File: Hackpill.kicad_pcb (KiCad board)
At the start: 2 copper layers, 63.2 x 30.5 mm, 34 parts, among them J1 Conn_01x04, J2 USB_C_Receptacle_USB2.0_16P, J3 Conn_01x22, J4 Conn_01x22, SW1 SW_Push, U1 STM32F042C6Tx, U2 AMS1117-3.3, U3 USBLC6-2SC6

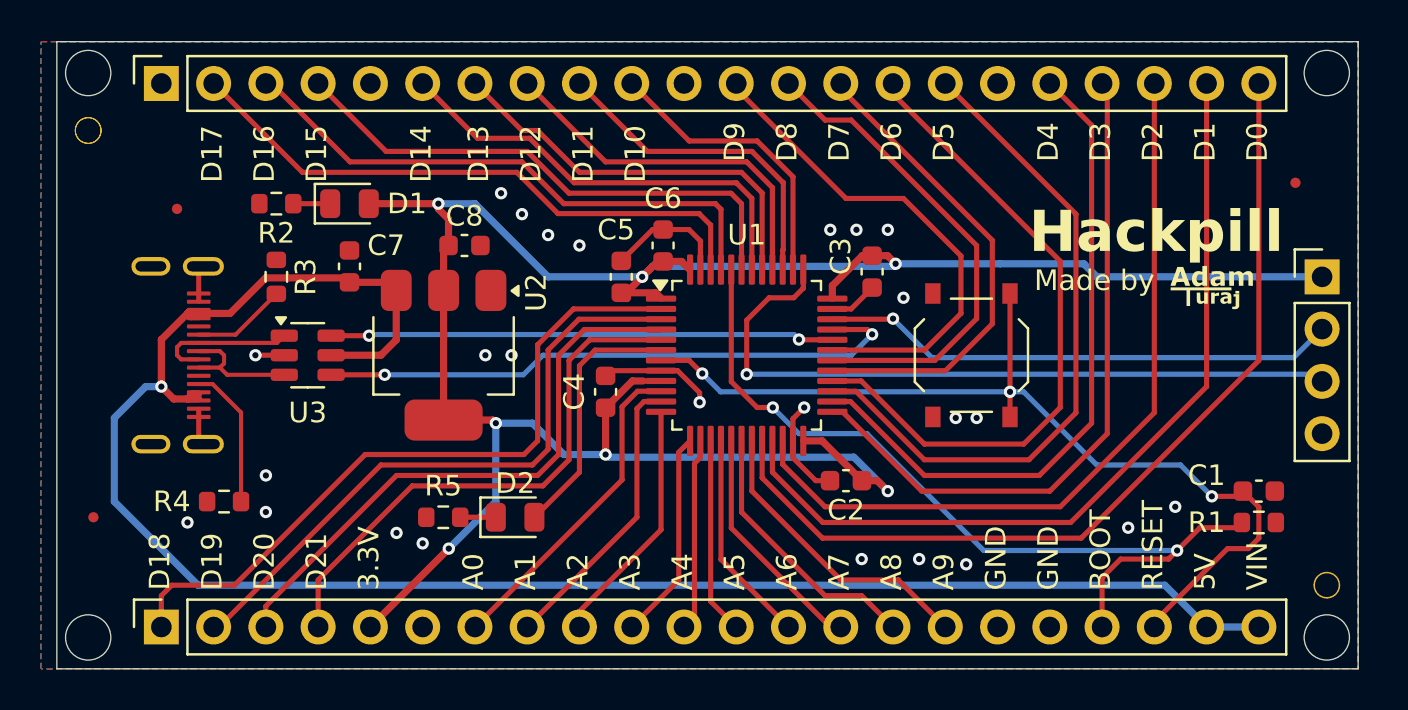
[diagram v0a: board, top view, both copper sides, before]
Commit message: Add diode to USB, rename files, add prod files
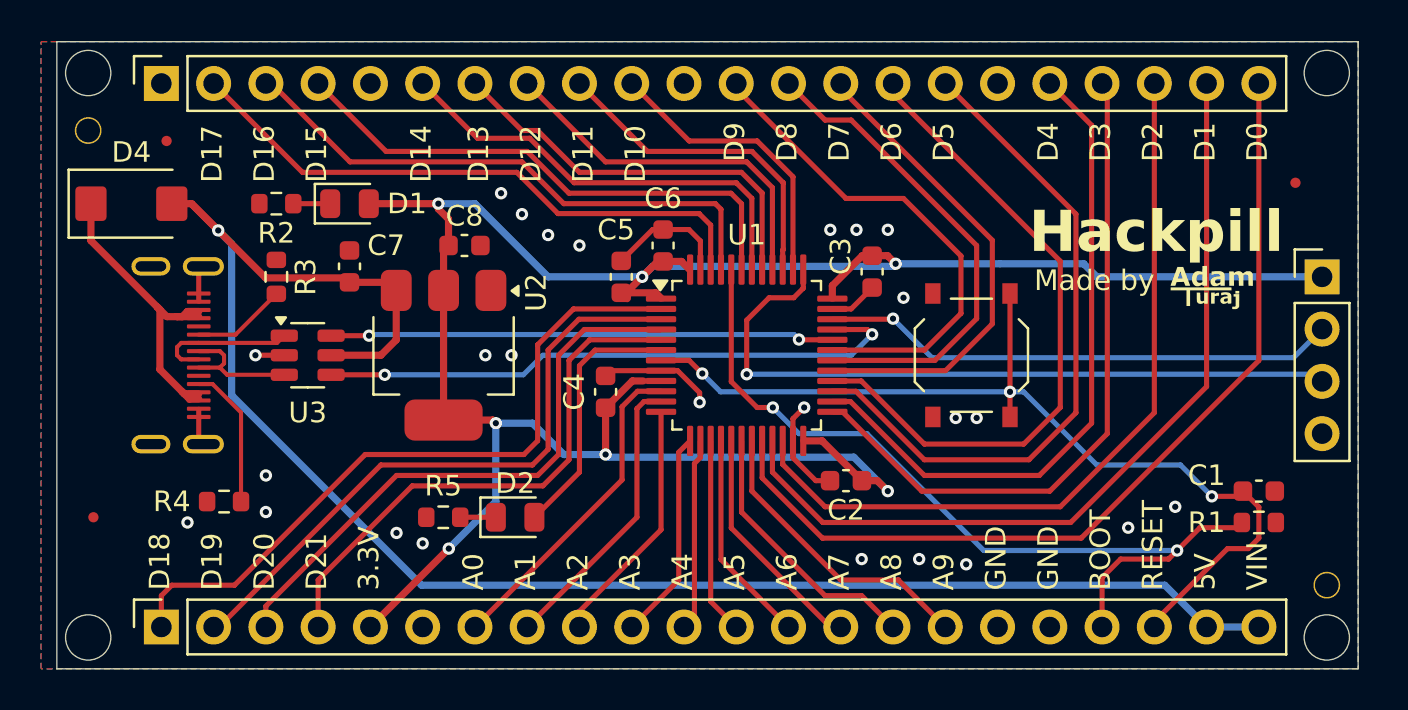
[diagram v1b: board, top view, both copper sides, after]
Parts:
- removed ?: , 
- added D4: SS14, Diode_SMD:D_SMA, F.Cu at (129.1, 93.0)
- moved REF** 3.34 mm to (130.8, 89.9)
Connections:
- J2 pad A4: +5V -> Net-(D4-A)
- J2 pad A9: +5V -> Net-(D4-A)
- J2 pad B4: +5V -> Net-(D4-A)
- J2 pad B9: +5V -> Net-(D4-A)
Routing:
- net Net-(D4-A): track 0.00 -> 16.1 mm
- net +5V: track 90.3 -> 83.4 mm

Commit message: Change clearence, update footprint, add README, add schematic, remove config file
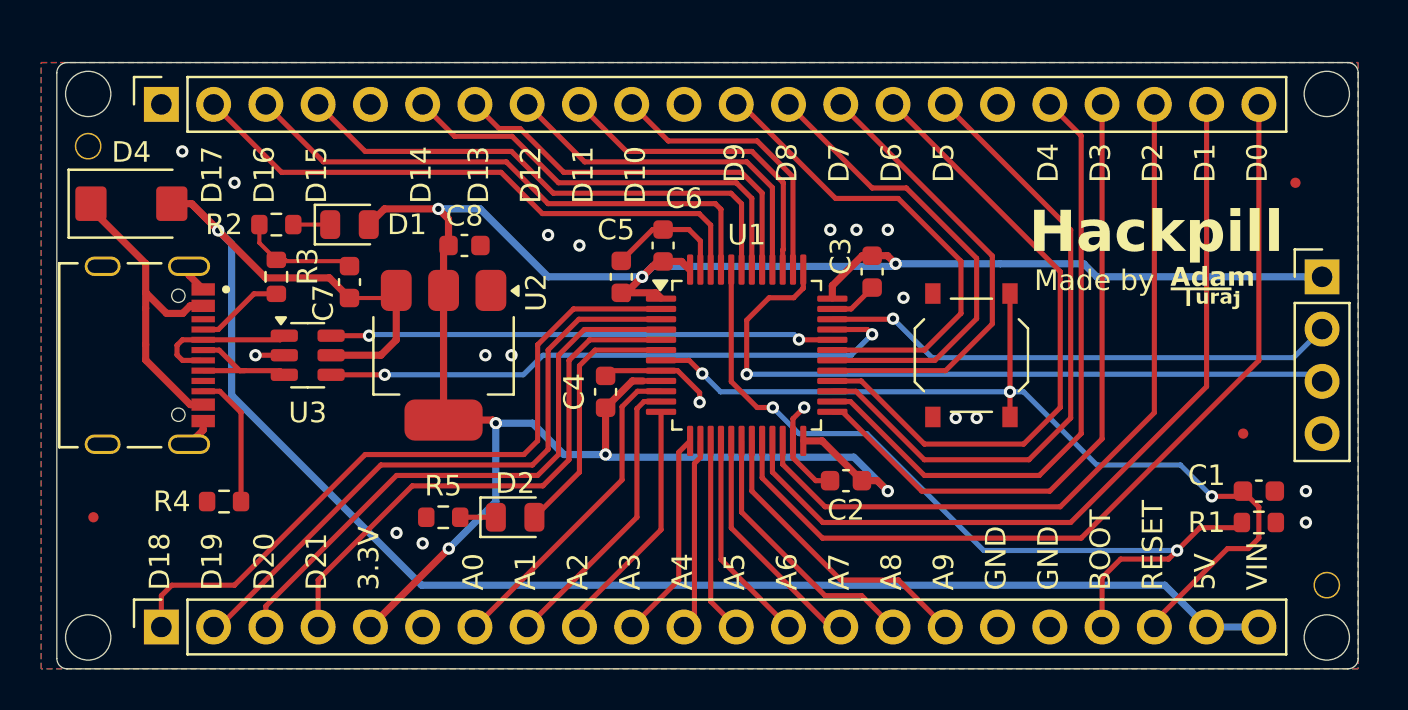
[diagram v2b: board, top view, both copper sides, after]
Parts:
- J2: footprint Connector_USB:USB_C_Receptacle_Hanbo_16P_TopMnt_Horizontal -> Connector_USB:USB_C_Receptacle_Shouhan_16P_TopMnt_Horizontal
- moved REF** 54.2 mm to (183.1, 104.1)
- moved J2 1.27 mm to (128.8, 100.3)
- moved D1 1.02 mm to (139.7, 94.0)
- moved J4 1.02 mm to (130.6, 88.1)
- moved R2 1.02 mm to (136.1, 94.0)
- moved REF** 1.02 mm to (187.2, 87.6)
- moved REF** 1.02 mm to (127.0, 87.6)
- moved C7 0.76 mm to (139.7, 96.8)
- moved REF** 0.76 mm to (127.0, 90.2)
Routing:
- net GND: track 24.0 -> 29.6 mm, vias 25 -> 19
- net D4: track 32.5 -> 31.1 mm
- net D5: track 32.8 -> 31.6 mm
- net D3: track 33.2 -> 32.0 mm
- net USART_TX_PWM_D9: track 24.8 -> 23.6 mm
- net D6: track 32.2 -> 31.2 mm
- net PWM_D7: track 23.5 -> 22.4 mm
- net I2C_SCL_PWM_D1: track 41.1 -> 40.1 mm
- net D0: track 44.2 -> 43.2 mm
- net I2C_SDA_PWM_D2: track 38.0 -> 36.9 mm
- net CAN_RX_PWM_D16: track 28.1 -> 27.2 mm
- net USART_TX_PWM_D8: track 23.8 -> 23.0 mm
- net +5V: track 83.4 -> 84.1 mm
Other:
- board size 63.2 x 30.5 mm -> 63.2 x 29.5 mm
